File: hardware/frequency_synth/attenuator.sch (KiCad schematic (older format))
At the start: 31 parts, among them U11 LTC1983, U12 HMC424, U13 74HC04_FULL

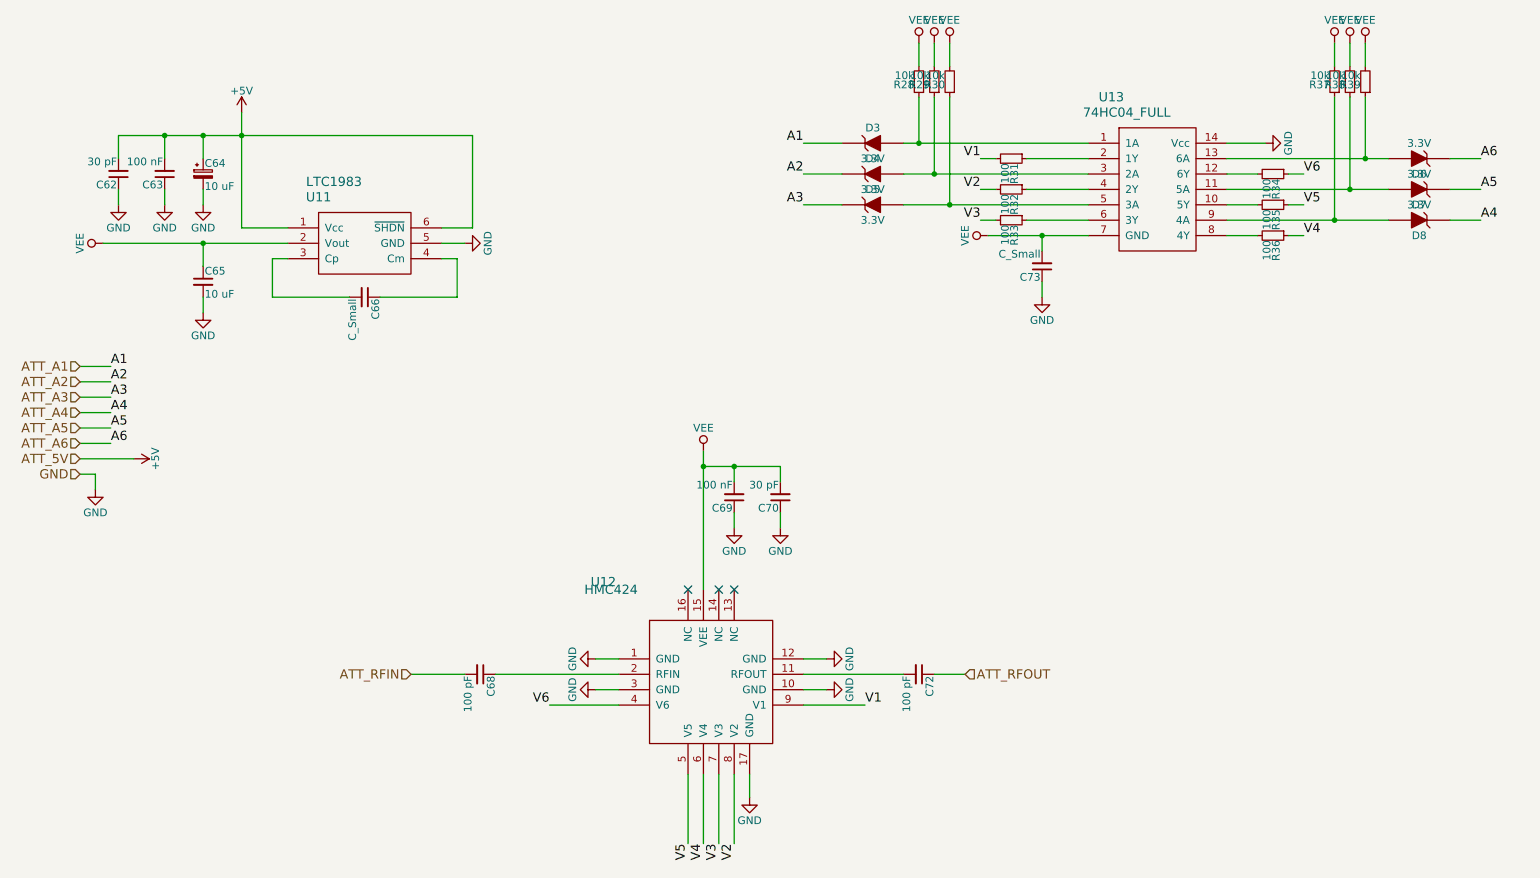
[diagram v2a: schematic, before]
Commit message: started on component placement
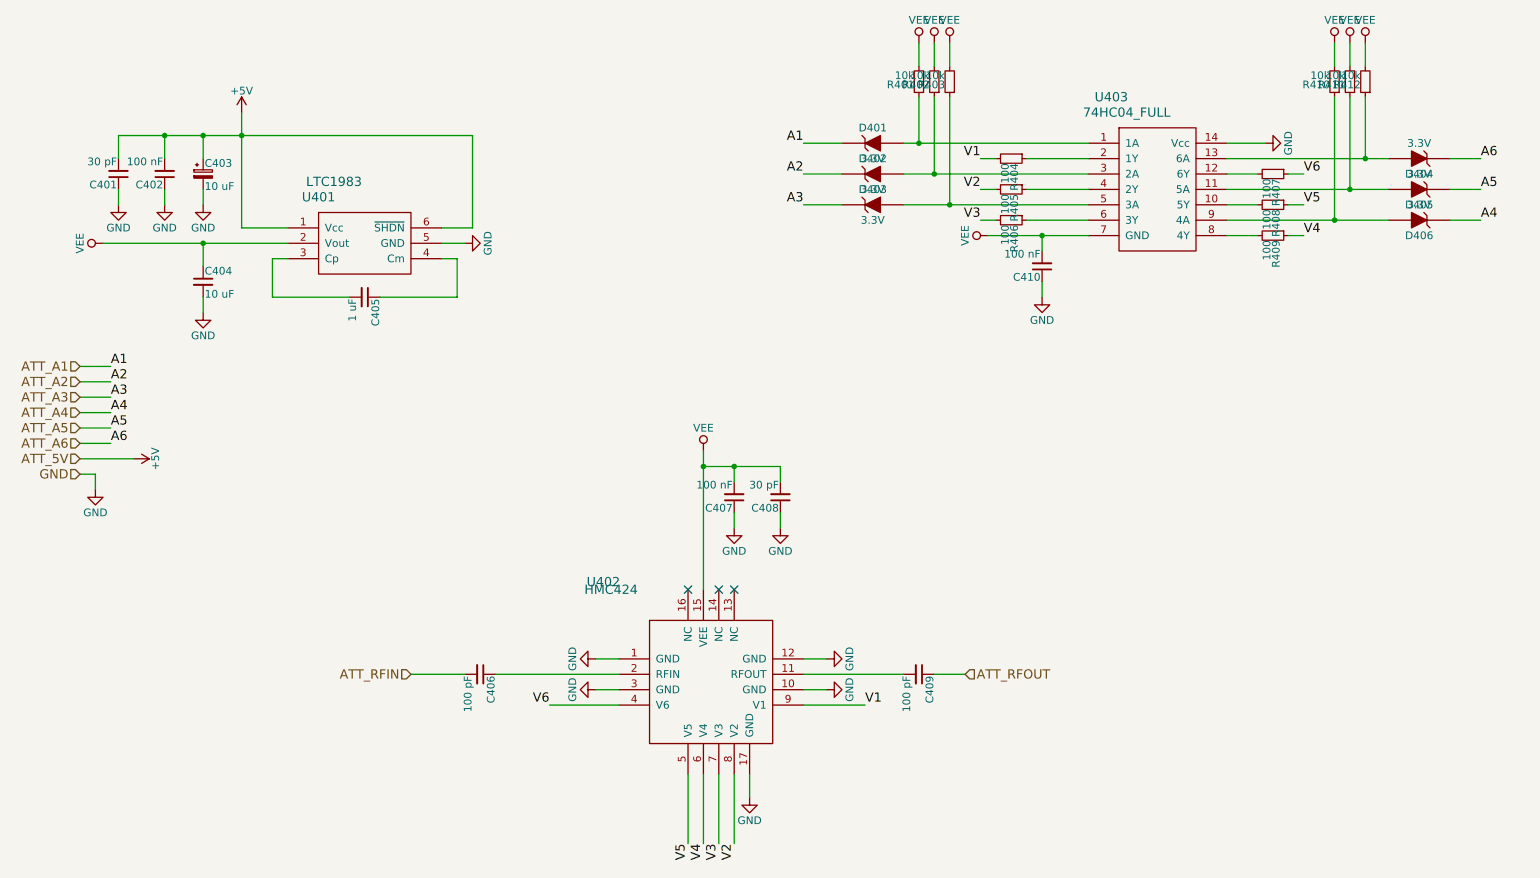
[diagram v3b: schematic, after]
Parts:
- C405: renamed from C66; value C_Small -> 1 uF; footprint Capacitors_SMD:C_0603 -> Capacitors_SMD:C_0402
- C410: renamed from C73; value C_Small -> 100 nF
- renumbered C62 to C401, C63 to C402, C64 to C403, C65 to C404, C68 to C406, C69 to C407, C70 to C408, C72 to C409, D3 to D401, D4 to D402, D5 to D403, D6 to D404, D7 to D405, D8 to D406, R28 to R401, R29 to R402, R30 to R403, R31 to R404, R32 to R405, R33 to R406, R34 to R407, R35 to R408, R36 to R409, R37 to R410, R38 to R411, R39 to R412, U11 to U401, U12 to U402, U13 to U403

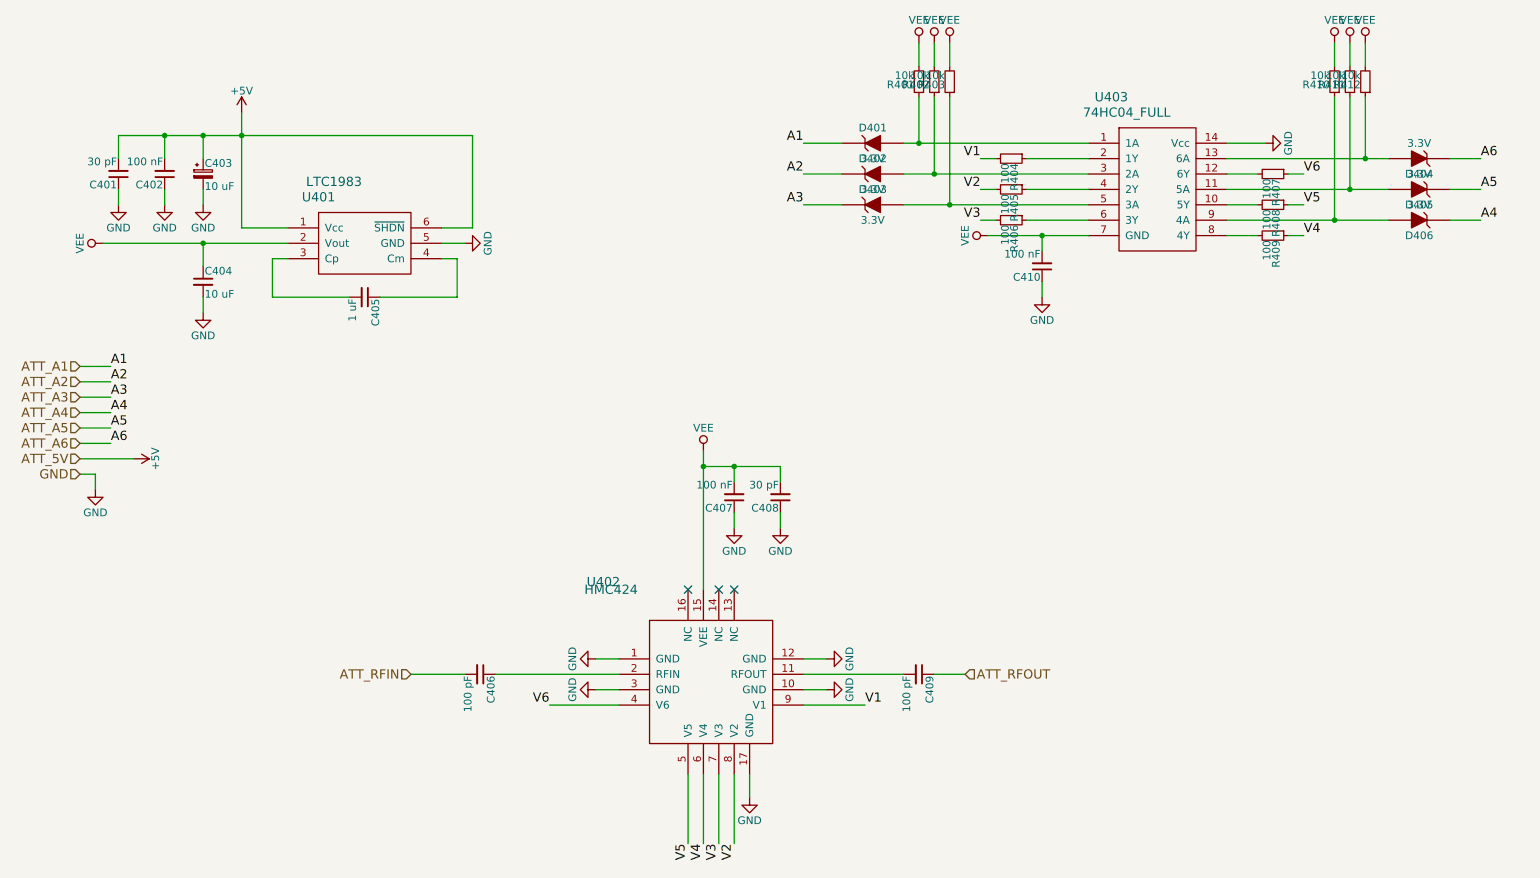
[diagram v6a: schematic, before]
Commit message: started on synth r1 (fixed r0 bugs..), component placement on ad9864 breakout
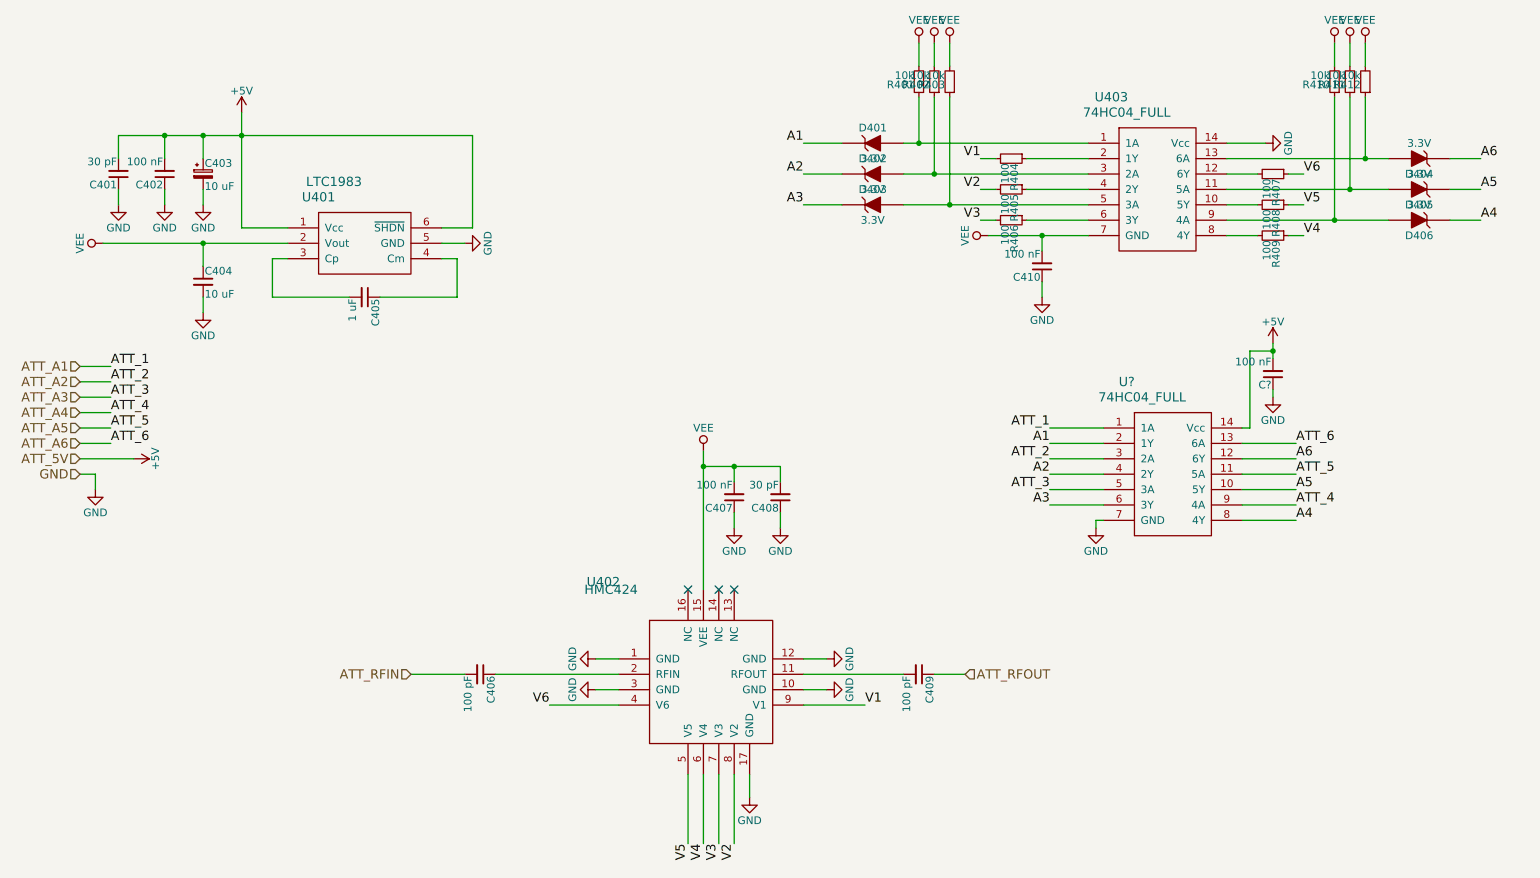
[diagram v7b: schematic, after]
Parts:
- added C?: 100 nF, Capacitors_SMD:C_0402, symbol C_Small
- added U?: 74HC04_FULL, Housings_SSOP:TSSOP-14_4.4x5mm_Pitch0.65mm, symbol 74HC04_FULL
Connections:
- net +5V: now also C?.2, U?.14 (Vcc)
- net ATT_A1: now also U?.1 (1A); no longer D401.1 (K)
- net ATT_A2: now also U?.3 (2A); no longer D402.1 (K)
- net ATT_A3: now also U?.5 (3A); no longer D403.1 (K)
- net ATT_A4: now also U?.9 (4A); no longer D406.1 (K)
- net ATT_A5: now also U?.11 (5A); no longer D405.1 (K)
- net ATT_A6: now also U?.13 (6A); no longer D404.1 (K)
- net GND: now also C?.1, U?.7 (GND)
- new net A1: D401.1 (K), U?.2 (1Y)
- new net A2: D402.1 (K), U?.4 (2Y)
- new net A3: D403.1 (K), U?.6 (3Y)
- new net A4: D406.1 (K), U?.8 (4Y)
- new net A5: D405.1 (K), U?.10 (5Y)
- new net A6: D404.1 (K), U?.12 (6Y)
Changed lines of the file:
@@
 $Descr A4 11693 8268
 encoding utf-8
-Sheet 4 10
+Sheet 4 9
 Title ""
 Date ""
@@
 $EndComp
 Text Label 1300 3250 0    60   ~ 0
-A1
+ATT_1
 Text Label 1300 3350 0    60   ~ 0
-A2
+ATT_2
 Text Label 1300 3550 0    60   ~ 0
-A4
+ATT_4
 Text Label 1300 3450 0    60   ~ 0
-A3
+ATT_3
 Text Label 1300 3650 0    60   ~ 0
-A5
+ATT_5
 Text Label 1300 3750 0    60   ~ 0
-A6
+ATT_6
 Wire Wire Line
 	1100 3250 1300 3250
@@
 Wire Wire Line
 	3250 5250 3600 5250
+$Comp
+L 74HC04_FULL U?
+U 1 1 57C3BD51
+P 8200 3950
+F 0 "U?" H 7900 4550 60  0000 C CNN
+F 1 "74HC04_FULL" H 8000 4450 60  0000 C CNN
+F 2 "Housings_SSOP:TSSOP-14_4.4x5mm_Pitch0.65mm" H 8200 3950 60  0001 C CNN
+F 3 "" H 8200 3950 60  0000 C CNN
+	1    8200 3950
+	1    0    0    -1
+$EndComp
+$Comp
+L C_Small C?
+U 1 1 57C3BF75
+P 8850 3300
+F 0 "C?" H 8860 3370 50  0000 L CNN
+F 1 "100 nF" H 8860 3220 50  0000 L CNN
+F 2 "Capacitors_SMD:C_0402" H 8850 3300 50  0001 C CNN
+F 3 "" H 8850 3300 50  0000 C CNN
+	1    8850 3300
+	-1   0    0    1
+$EndComp
+$Comp
+L GND #PWR?
+U 1 1 57C3C099
+P 8850 3450
+F 0 "#PWR?" H 8850 3200 50  0001 C CNN
+F 1 "GND" H 8850 3300 50  0000 C CNN
+F 2 "" H 8850 3450 50  0000 C CNN
+F 3 "" H 8850 3450 50  0000 C CNN
+	1    8850 3450
+	1    0    0    -1
+$EndComp
+Wire Wire Line
+	8850 3400 8850 3450
+$Comp
+L +5V #PWR?
+U 1 1 57C3C52B
+P 8850 3100
+F 0 "#PWR?" H 8850 2950 50  0001 C CNN
+F 1 "+5V" H 8850 3240 50  0000 C CNN
+F 2 "" H 8850 3100 50  0000 C CNN
+F 3 "" H 8850 3100 50  0000 C CNN
+	1    8850 3100
+	1    0    0    -1
+$EndComp
+Wire Wire Line
+	8850 3100 8850 3200
+Wire Wire Line
+	8850 3150 8700 3150
+Wire Wire Line
+	8700 3150 8700 3650
+Wire Wire Line
+	8700 3650 8650 3650
+Connection ~ 8850 3150
+$Comp
+L GND #PWR?
+U 1 1 57C3CA74
+P 7700 4300
+F 0 "#PWR?" H 7700 4050 50  0001 C CNN
+F 1 "GND" H 7700 4150 50  0000 C CNN
+F 2 "" H 7700 4300 50  0000 C CNN
+F 3 "" H 7700 4300 50  0000 C CNN
+	1    7700 4300
+	1    0    0    -1
+$EndComp
+Wire Wire Line
+	7750 4250 7700 4250
+Wire Wire Line
+	7700 4250 7700 4300
+Text Label 7400 3750 2    60   ~ 0
+A1
+Wire Wire Line
+	7400 3750 7750 3750
+Wire Wire Line
+	7400 3650 7750 3650
+Text Label 7400 3650 2    60   ~ 0
+ATT_1
+Text Label 7400 3850 2    60   ~ 0
+ATT_2
+Wire Wire Line
+	7400 3850 7750 3850
+Text Label 7400 3950 2    60   ~ 0
+A2
+Wire Wire Line
+	7400 3950 7750 3950
+Text Label 7400 4050 2    60   ~ 0
+ATT_3
+Text Label 7400 4150 2    60   ~ 0
+A3
+Wire Wire Line
+	7400 4150 7750 4150
+Wire Wire Line
+	7400 4050 7750 4050
+Text Label 9000 3850 0    60   ~ 0
+A6
+Wire Wire Line
+	9000 3850 8650 3850
+Wire Wire Line
+	9000 3750 8650 3750
+Text Label 9000 3750 0    60   ~ 0
+ATT_6
+Text Label 9000 3950 0    60   ~ 0
+ATT_5
+Wire Wire Line
+	9000 3950 8650 3950
+Text Label 9000 4050 0    60   ~ 0
+A5
+Wire Wire Line
+	9000 4050 8650 4050
+Text Label 9000 4150 0    60   ~ 0
+ATT_4
+Text Label 9000 4250 0    60   ~ 0
+A4
+Wire Wire Line
+	9000 4250 8650 4250
+Wire Wire Line
+	9000 4150 8650 4150
 $EndSCHEMATC
